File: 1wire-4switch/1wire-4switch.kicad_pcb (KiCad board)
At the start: 2 copper layers, 74.7 x 59.4 mm, 20 parts, among them IC1 DS2408S, J1 RJ45, J2 RJ45, K1 CONN_3, K2 CONN_3, P1 CONN_4, P2 CONN_4, P3 CONN_5_V, P4 CONN_4, U1 74HC04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

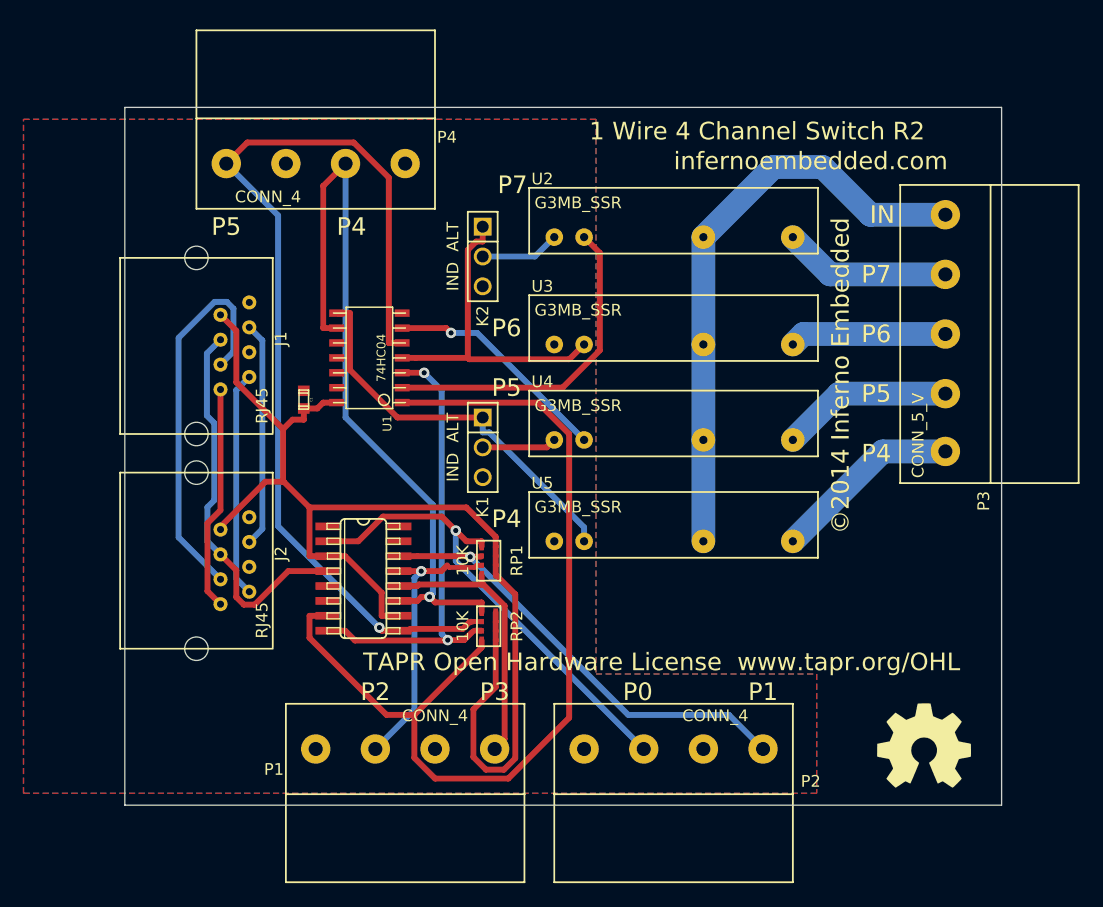
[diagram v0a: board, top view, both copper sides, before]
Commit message: Increased hole size for connectors Compacted the board a little bit RJ45 sockets now overhang the board in order to sit flust with the case
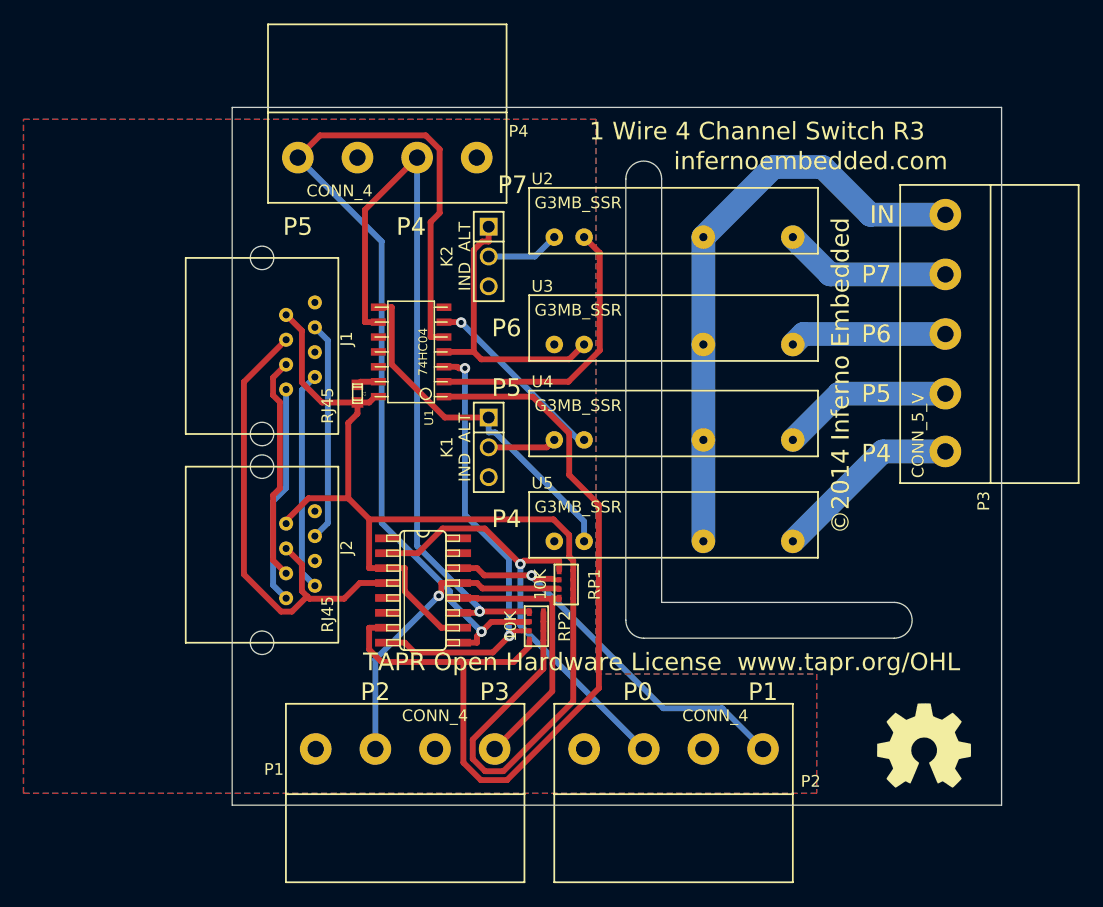
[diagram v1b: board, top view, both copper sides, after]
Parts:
- removed ? (x2): , slot
- moved RP1 6.91 mm to (115.3, 139.7)
- moved P4 6.12 mm to (89.9, 107.2)
- moved J2 5.61 mm to (89.4, 137.2)
- moved J1 5.59 mm to (89.4, 119.4)
- moved IC1 5.18 mm to (103.1, 140.2)
- moved C1 4.60 mm to (97.5, 123.4)
- moved RP2 4.06 mm to (112.8, 143.3)
- moved U1 3.59 mm to (102.1, 119.9)
- moved K1 0.51 mm to (108.7, 128.0)
- moved K2 0.51 mm to (108.7, 111.8)
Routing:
- net N-0000021: track 33.5 -> 19.2 mm
- net N-0000022: track 33.1 -> 41.0 mm
- net N-000003: track 83.0 -> 77.2 mm
- net N-0000029: track 38.8 -> 34.8 mm
- net N-000008: track 28.1 -> 24.2 mm
- net N-000009: track 28.3 -> 24.6 mm
- net N-000002: track 19.4 -> 16.1 mm
- net N-000001: track 33.4 -> 30.4 mm
- net N-0000027: track 40.6 -> 37.8 mm
- net VCC: track 101.9 -> 104.5 mm
- net N-0000030: track 24.1 -> 26.7 mm
- net GND: track 0.00 -> 1.89 mm
- net N-0000024: track 19.2 -> 18.7 mm
- net N-0000019: track 19.2 -> 18.7 mm
- net N-0000020: track 19.2 -> 18.7 mm
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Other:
- board size 74.7 x 59.4 mm -> 65.5 x 59.4 mm
- board text added: "1 Wire 4 Channel Switch R3"
- board text removed: "1 Wire 4 Channel Switch R2"

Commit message: Move back the external connectors to afford more clearance for right angled connectors Fix the reversed pinouts on the PJ45 connectors
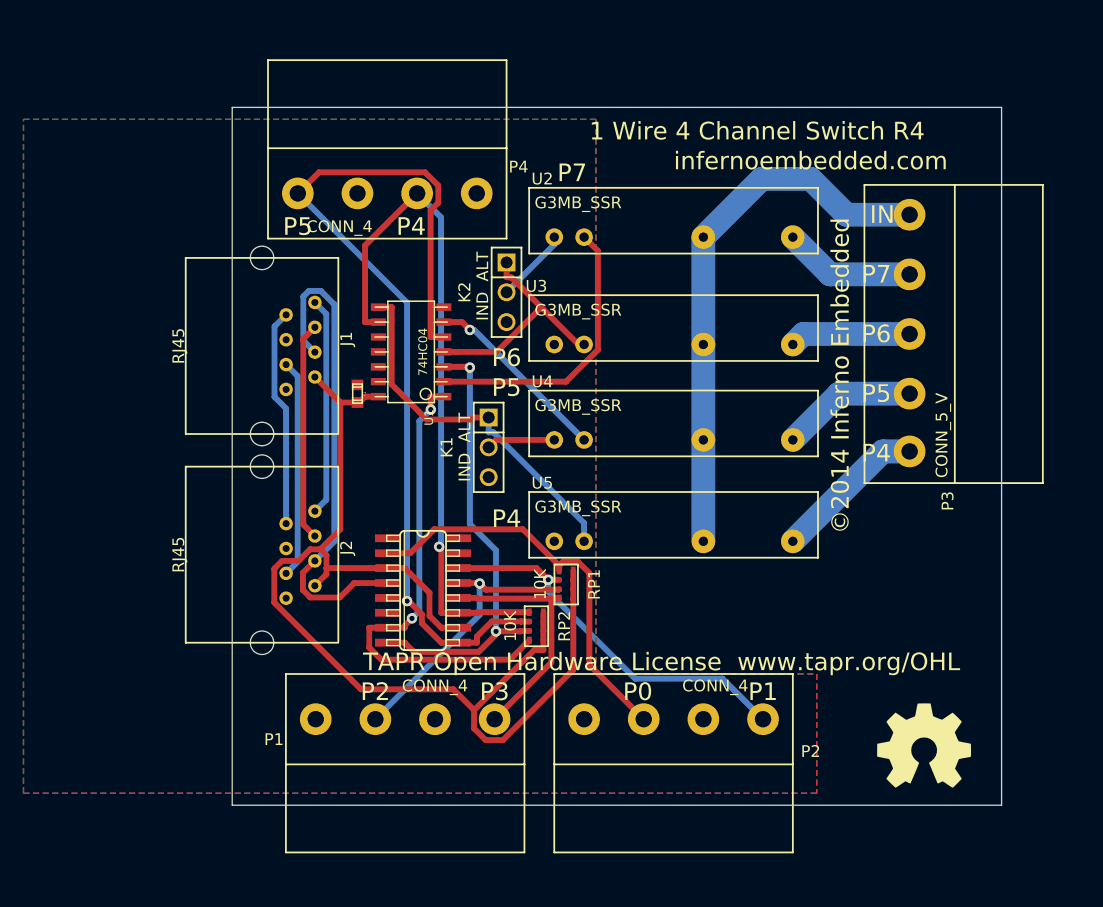
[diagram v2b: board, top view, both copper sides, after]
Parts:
- moved K2 3.41 mm to (110.2, 114.8)
- moved P3 3.05 mm to (140.7, 105.7)
- moved P4 3.05 mm to (89.9, 110.2)
- moved P1 2.54 mm to (111.8, 147.3)
- moved P2 2.54 mm to (134.6, 147.3)
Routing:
- net N-000003: track 77.2 -> 41.2 mm, vias 0 -> 2
- net N-0000013: track 63.9 -> 58.2 mm
- net VCC: track 104.5 -> 98.9 mm
- net N-0000014: track 84.7 -> 79.5 mm
- net N-000008: track 24.2 -> 20.1 mm
- net /Mains_In: track 50.7 -> 46.8 mm
- net N-0000027: track 37.8 -> 34.7 mm, vias 1 -> 0
- net /OUT_3: track 14.6 -> 11.6 mm
- net /OUT_2: track 13.4 -> 10.3 mm
- net /OUT_1: track 14.3 -> 11.3 mm
- net /OUT_4: track 16.2 -> 13.1 mm
- net N-0000030: track 26.7 -> 24.0 mm
- net N-0000023: track 23.4 -> 20.8 mm
- net N-0000029: track 34.8 -> 32.7 mm
- net GND: track 1.89 -> 0.00 mm
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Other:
- outline, holes or cut-outs redrawn
- net class Default: clearance 0.254 -> 0.15
- rule pad_to_mask_clearance: 0 -> 0.1
- rule trace_clearance: 0.254 -> 0.15
- board text added: "1 Wire 4 Channel Switch R4"
- board text removed: "1 Wire 4 Channel Switch R3"
